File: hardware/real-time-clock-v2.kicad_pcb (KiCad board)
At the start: 2 copper layers, 25 x 25 mm, 28 parts, among them P1 CON-SENSOR, P2 Debug, P3 Boot, U1 XMC1100, U2 PCF85263AT, U3 DRILL, U4 DRILL, U5 DRILL, U6 DRILL, X1 32.768kHz

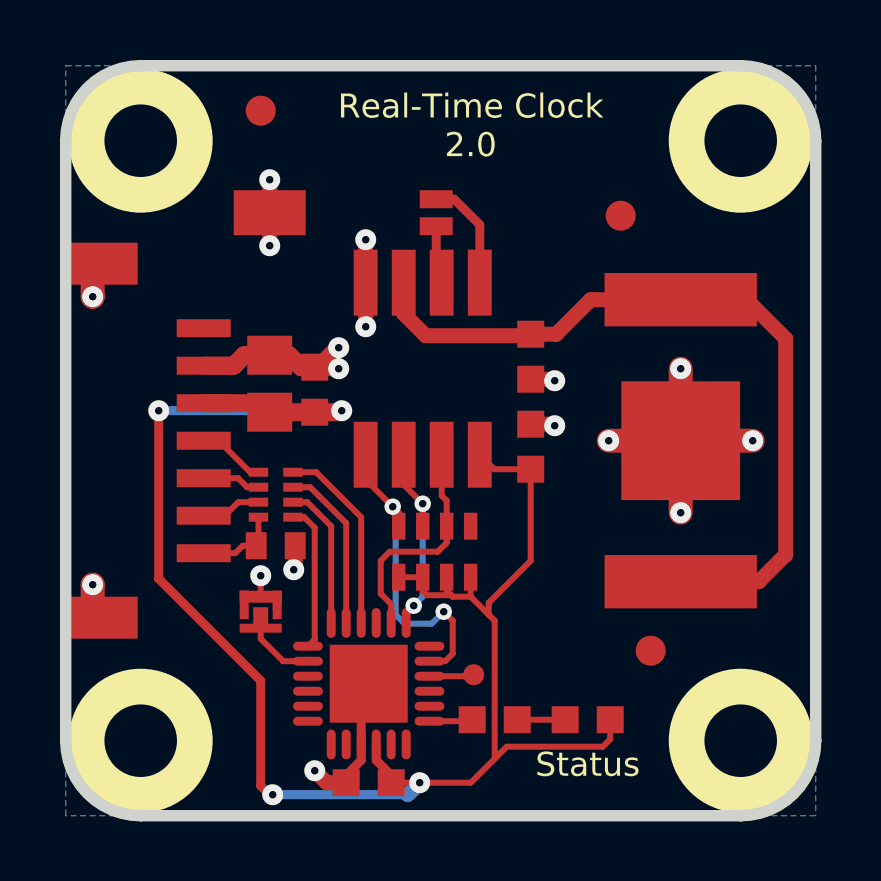
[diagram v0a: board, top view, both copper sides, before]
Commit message: Change capacitor footprint(s) to C0402F 78634
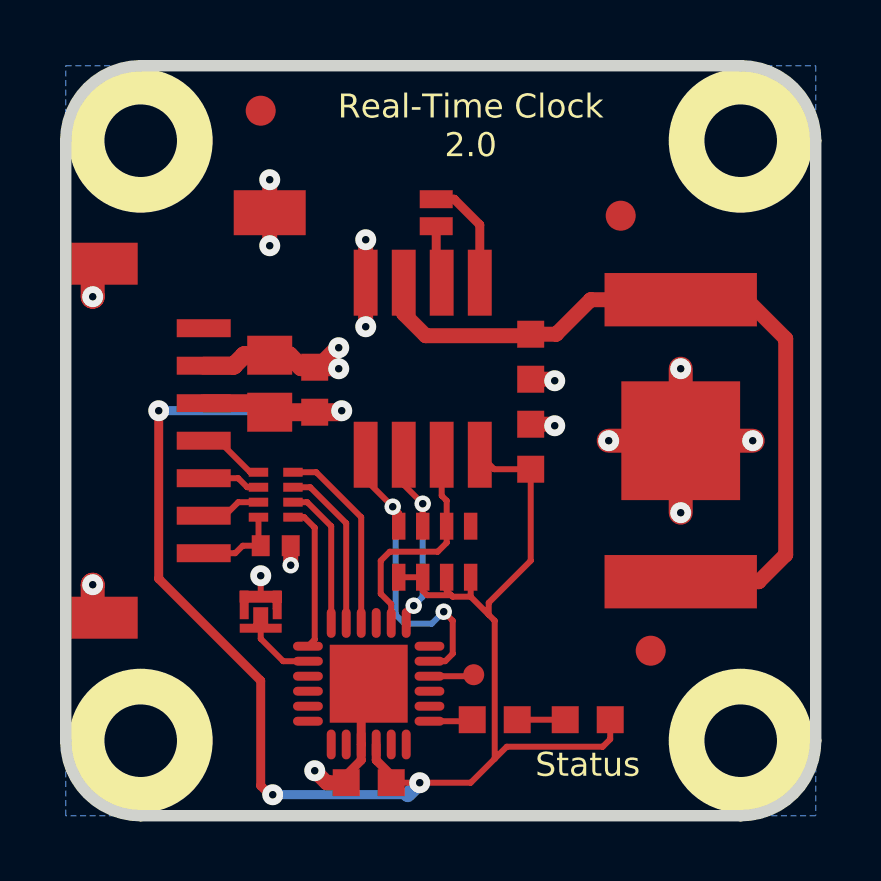
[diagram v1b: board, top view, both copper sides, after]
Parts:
- C1: footprint kicad-libraries:C0402E -> kicad-libraries:C0402F
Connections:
- P1 pad 1: (no net) -> Net-(P1-Pad1)
- RP2 pad 4: (no net) -> Net-(RP2-Pad4)
- U1 pad 11: (no net) -> Net-(U1-Pad11)
- U1 pad 12: (no net) -> Net-(U1-Pad12)
- U1 pad 14: (no net) -> Net-(U1-Pad14)
- U1 pad 15: (no net) -> Net-(U1-Pad15)
- U1 pad 18: (no net) -> Net-(U1-Pad18)
- U1 pad 21: (no net) -> Net-(U1-Pad21)
- U1 pad 3: (no net) -> Net-(U1-Pad3)
- U1 pad 4: (no net) -> Net-(U1-Pad4)
- U1 pad 5: (no net) -> Net-(U1-Pad5)
- U1 pad 6: (no net) -> Net-(U1-Pad6)
- U1 pad 7: (no net) -> Net-(U1-Pad7)
- U1 pad 8: (no net) -> Net-(U1-Pad8)
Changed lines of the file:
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@@
     (thickness 1.6002)
     (drawings 12)
-    (tracks 198)
+    (tracks 197)
     (zones 0)
     (modules 28)
-    (nets 21)
+    (nets 35)
   )
   (page A4)
@@
   )
   (layers
-    (0 Vorderseite signal hide)
-    (31 Rückseite signal hide)
+    (0 Vorderseite signal)
+    (31 Rückseite signal)
     (32 B.Adhes user)
     (33 F.Adhes user)
@@
   )
   (setup
-    (last_trace_width 0.249)
+    (last_trace_width 0.5)
     (user_trace_width 0.2)
     (user_trace_width 0.25)
@@
   (net 19 INT)
   (net 20 "Net-(R1-Pad1)")
+  (net 21 "Net-(P1-Pad1)")
+  (net 22 "Net-(RP2-Pad4)")
+  (net 23 "Net-(U1-Pad3)")
+  (net 24 "Net-(U1-Pad4)")
+  (net 25 "Net-(U1-Pad5)")
+  (net 26 "Net-(U1-Pad6)")
+  (net 27 "Net-(U1-Pad7)")
+  (net 28 "Net-(U1-Pad8)")
+  (net 29 "Net-(U1-Pad11)")
+  (net 30 "Net-(U1-Pad12)")
+  (net 31 "Net-(U1-Pad14)")
+  (net 32 "Net-(U1-Pad15)")
+  (net 33 "Net-(U1-Pad18)")
+  (net 34 "Net-(U1-Pad21)")
   (net_class Default "Dies ist die voreingestellte Netzklasse."
     (clearance 0.14986)
@@
     (add_net "Net-(C1-Pad1)")
     (add_net "Net-(D1-Pad2)")
+    (add_net "Net-(P1-Pad1)")
     (add_net "Net-(P1-Pad4)")
     (add_net "Net-(P1-Pad5)")
@@
     (add_net "Net-(P3-Pad2)")
     (add_net "Net-(R1-Pad1)")
+    (add_net "Net-(RP2-Pad4)")
+    (add_net "Net-(U1-Pad11)")
+    (add_net "Net-(U1-Pad12)")
+    (add_net "Net-(U1-Pad14)")
+    (add_net "Net-(U1-Pad15)")
+    (add_net "Net-(U1-Pad18)")
+    (add_net "Net-(U1-Pad21)")
+    (add_net "Net-(U1-Pad3)")
+    (add_net "Net-(U1-Pad4)")
+    (add_net "Net-(U1-Pad5)")
+    (add_net "Net-(U1-Pad6)")
+    (add_net "Net-(U1-Pad7)")
+    (add_net "Net-(U1-Pad8)")
     (add_net "Net-(U2-Pad1)")
     (add_net "Net-(U2-Pad2)")
@@
     (pad 2 smd oval (at -2.025 -0.75) (size 1 0.3) (layers Vorderseite F.Paste F.Mask)
       (net 14 "Net-(P3-Pad2)"))
-    (pad 3 smd oval (at -2.025 -0.25) (size 1 0.3) (layers Vorderseite F.Paste F.Mask))
-    (pad 4 smd oval (at -2.025 0.25) (size 1 0.3) (layers Vorderseite F.Paste F.Mask))
-    (pad 5 smd oval (at -2.025 0.75) (size 1 0.3) (layers Vorderseite F.Paste F.Mask))
-    (pad 6 smd oval (at -2.025 1.25) (size 1 0.3) (layers Vorderseite F.Paste F.Mask))
-    (pad 7 smd oval (at -1.25 2.025 90) (size 1 0.3) (layers Vorderseite F.Paste F.Mask))
-    (pad 8 smd oval (at -0.75 2.025 90) (size 1 0.3) (layers Vorderseite F.Paste F.Mask))
+    (pad 3 smd oval (at -2.025 -0.25) (size 1 0.3) (layers Vorderseite F.Paste F.Mask)
+      (net 23 "Net-(U1-Pad3)"))
+    (pad 4 smd oval (at -2.025 0.25) (size 1 0.3) (layers Vorderseite F.Paste F.Mask)
+      (net 24 "Net-(U1-Pad4)"))
+    (pad 5 smd oval (at -2.025 0.75) (size 1 0.3) (layers Vorderseite F.Paste F.Mask)
+      (net 25 "Net-(U1-Pad5)"))
+    (pad 6 smd oval (at -2.025 1.25) (size 1 0.3) (layers Vorderseite F.Paste F.Mask)
+      (net 26 "Net-(U1-Pad6)"))
+    (pad 7 smd oval (at -1.25 2.025 90) (size 1 0.3) (layers Vorderseite F.Paste F.Mask)
+      (net 27 "Net-(U1-Pad7)"))
+    (pad 8 smd oval (at -0.75 2.025 90) (size 1 0.3) (layers Vorderseite F.Paste F.Mask)
+      (net 28 "Net-(U1-Pad8)"))
     (pad 9 smd oval (at -0.25 2.025 90) (size 1 0.3) (layers Vorderseite F.Paste F.Mask)
       (net 1 GND))
     (pad 10 smd oval (at 0.25 2.025 90) (size 1 0.3) (layers Vorderseite F.Paste F.Mask)
       (net 7 3V3))
-    (pad 11 smd oval (at 0.75 2.025 90) (size 1 0.3) (layers Vorderseite F.Paste F.Mask))
-    (pad 12 smd oval (at 1.25 2.025 90) (size 1 0.3) (layers Vorderseite F.Paste F.Mask))
+    (pad 11 smd oval (at 0.75 2.025 90) (size 1 0.3) (layers Vorderseite F.Paste F.Mask)
+      (net 29 "Net-(U1-Pad11)"))
+    (pad 12 smd oval (at 1.25 2.025 90) (size 1 0.3) (layers Vorderseite F.Paste F.Mask)
+      (net 30 "Net-(U1-Pad12)"))
     (pad 13 smd oval (at 2.025 1.25) (size 1 0.3) (layers Vorderseite F.Paste F.Mask)
       (net 20 "Net-(R1-Pad1)"))
-    (pad 14 smd oval (at 2.025 0.75) (size 1 0.3) (layers Vorderseite F.Paste F.Mask))
-    (pad 15 smd oval (at 2.025 0.25) (size 1 0.3) (layers Vorderseite F.Paste F.Mask))
+    (pad 14 smd oval (at 2.025 0.75) (size 1 0.3) (layers Vorderseite F.Paste F.Mask)
+      (net 31 "Net-(U1-Pad14)"))
+    (pad 15 smd oval (at 2.025 0.25) (size 1 0.3) (layers Vorderseite F.Paste F.Mask)
+      (net 32 "Net-(U1-Pad15)"))
     (pad 16 smd oval (at 2.025 -0.25) (size 1 0.3) (layers Vorderseite F.Paste F.Mask)
       (net 13 "Net-(P2-Pad1)"))
     (pad 17 smd oval (at 2.025 -0.75) (size 1 0.3) (layers Vorderseite F.Paste F.Mask)
       (net 3 SDA))
-    (pad 18 smd oval (at 2.025 -1.25) (size 1 0.3) (layers Vorderseite F.Paste F.Mask))
+    (pad 18 smd oval (at 2.025 -1.25) (size 1 0.3) (layers Vorderseite F.Paste F.Mask)
+      (net 33 "Net-(U1-Pad18)"))
     (pad 19 smd oval (at 1.25 -2.025 90) (size 1 0.3) (layers Vorderseite F.Paste F.Mask)
       (net 2 SCL))
     (pad 20 smd oval (at 0.75 -2.025 90) (size 1 0.3) (layers Vorderseite F.Paste F.Mask)
       (net 19 INT))
-    (pad 21 smd oval (at 0.25 -2.025 90) (size 1 0.3) (layers Vorderseite F.Paste F.Mask))
+    (pad 21 smd oval (at 0.25 -2.025 90) (size 1 0.3) (layers Vorderseite F.Paste F.Mask)
+      (net 34 "Net-(U1-Pad21)"))
     (pad 22 smd oval (at -0.25 -2.025 90) (size 1 0.3) (layers Vorderseite F.Paste F.Mask)
       (net 18 S-CS))
@@
     (pad 3 smd rect (at 0.39878 -0.8509) (size 0.44958 0.89916) (layers Vorderseite F.Paste F.Mask)
       (net 19 INT))
-    (pad 4 smd rect (at 1.19888 -0.8509) (size 0.44958 0.89916) (layers Vorderseite F.Paste F.Mask))
+    (pad 4 smd rect (at 1.19888 -0.8509) (size 0.44958 0.89916) (layers Vorderseite F.Paste F.Mask)
+      (net 22 "Net-(RP2-Pad4)"))
     (pad 5 smd rect (at 1.19888 0.8509) (size 0.44958 0.89916) (layers Vorderseite F.Paste F.Mask)
       (net 7 3V3))
@@
     (fp_line (start 6 -4.3) (end -6 -4.3) (layer F.Fab) (width 0.05))
     (fp_line (start -6 -4.3) (end -6 -0.25) (layer F.Fab) (width 0.05))
-    (pad 1 smd rect (at -3.75 -4.6 270) (size 0.6 1.8) (layers Vorderseite F.Paste F.Mask))
+    (pad 1 smd rect (at -3.75 -4.6 270) (size 0.6 1.8) (layers Vorderseite F.Paste F.Mask)
+      (net 21 "Net-(P1-Pad1)"))
     (pad 2 smd rect (at -2.5 -4.6 270) (size 0.6 1.8) (layers Vorderseite F.Paste F.Mask)
       (net 1 GND))
@@
     )
   )
-  (module kicad-libraries:C0402E (layer Vorderseite)
-    (at 132.3 104.1)
-    (attr smd)
-    (fp_text reference C1 (at 0 0.125) (layer F.Fab)
-      (effects (font (size 0.2 0.2) (thickness 0.05)))
-    )
-    (fp_text value 220pF (at 0 -0.275) (layer F.Fab)
-      (effects (font (size 0.2 0.2) (thickness 0.05)))
-    )
-    (fp_line (start -0.8509 -0.44958) (end 0.8509 -0.44958) (layer F.Fab) (width 0.001))
-    (fp_line (start 0.8509 -0.44958) (end 0.8509 0.44958) (layer F.Fab) (width 0.001))
-    (fp_line (start 0.8509 0.44958) (end -0.8509 0.44958) (layer F.Fab) (width 0.001))
-    (fp_line (start -0.8509 0.44958) (end -0.8509 -0.44958) (layer F.Fab) (width 0.001))
-    (pad 1 smd rect (at -0.65 0) (size 0.7 0.9) (layers Vorderseite F.Paste F.Mask)
-      (net 9 "Net-(C1-Pad1)"))
-    (pad 2 smd rect (at 0.65 0) (size 0.7 0.9) (layers Vorderseite F.Paste F.Mask)
-      (net 1 GND))
-    (model Capacitors_SMD/C_0402.wrl
-      (at (xyz 0 0 0))
-      (scale (xyz 1 1 1))
-      (rotate (xyz 0 0 0))
-    )
-  )
   (module kicad-libraries:Fiducial_Mark (layer Vorderseite)
     (at 143.8 93.1)
@@
     )
   )
+  (module kicad-libraries:C0402F (layer Vorderseite)
+    (at 132.3 104.1)
+    (fp_text reference C1 (at 0.1 0.15) (layer F.Fab)
+      (effects (font (size 0.2 0.2) (thickness 0.05)))
+    )
+    (fp_text value 220pF (at 0 -0.15) (layer F.Fab)
+      (effects (font (size 0.2 0.2) (thickness 0.05)))
+    )
+    (fp_line (start -0.9 -0.45) (end 0.9 -0.45) (layer F.Fab) (width 0.025))
+    (fp_line (start 0.9 -0.45) (end 0.9 0.45) (layer F.Fab) (width 0.025))
+    (fp_line (start 0.9 0.45) (end -0.9 0.45) (layer F.Fab) (width 0.025))
+    (fp_line (start -0.9 0.45) (end -0.9 -0.45) (layer F.Fab) (width 0.025))
+    (pad 2 smd rect (at 0.5 0) (size 0.6 0.7) (layers Vorderseite F.Paste F.Mask)
+      (net 1 GND))
+    (pad 1 smd rect (at -0.5 0) (size 0.6 0.7) (layers Vorderseite F.Paste F.Mask)
+      (net 9 "Net-(C1-Pad1)"))
+    (model Capacitors_SMD/C_0402.wrl
+      (at (xyz 0 0 0))
+      (scale (xyz 1 1 1))
+      (rotate (xyz 0 0 0))
+    )
+  )
   (gr_text Status (at 142.7 111.4) (layer F.SilkS)
     (effects (font (size 0.8001 0.8001) (thickness 0.14986)))
@@
     (effects (font (size 0.8001 0.8001) (thickness 0.14986)))
   )
+  (segment (start 132.8 104.1) (end 132.8 104.75) (width 0.5) (layer Vorderseite) (net 1) (status 400000))
+  (via (at 132.8 104.75) (size 0.55) (drill 0.25) (layers Vorderseite Rückseite) (net 1))
   (segment (start 131.8 105.8) (end 132.3 105.8) (width 0.2) (layer Vorderseite) (net 1))
   (segment (start 132.3 105.8) (end 132.3 106.2) (width 0.2) (layer Vorderseite) (net 1))
@@
   (segment (start 131.8 105.8) (end 131.8 105.1) (width 0.2) (layer Vorderseite) (net 1))
   (via (at 131.8 105.1) (size 0.7) (drill 0.25) (layers Vorderseite Rückseite) (net 1))
-  (segment (start 132.95 104.1) (end 132.95 104.85) (width 0.5) (layer Vorderseite) (net 1))
-  (via (at 132.9 104.9) (size 0.7) (drill 0.25) (layers Vorderseite Rückseite) (net 1))
-  (segment (start 132.95 104.85) (end 132.9 104.9) (width 0.5) (layer Vorderseite) (net 1))
   (segment (start 132.1 93) (end 132.1 91.9) (width 0.5) (layer Vorderseite) (net 1))
   (via (at 132.1 91.9) (size 0.7) (drill 0.25) (layers Vorderseite Rückseite) (net 1))
